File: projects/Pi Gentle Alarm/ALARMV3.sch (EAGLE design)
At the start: 9 parts, among them IC1 7805T, X1 RASPI_BOARD_B+_E0

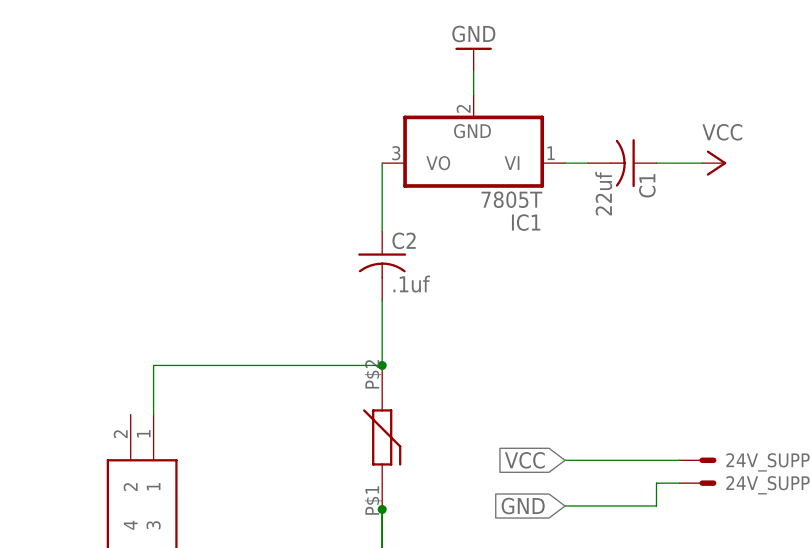
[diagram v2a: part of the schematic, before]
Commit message: Removed extra components
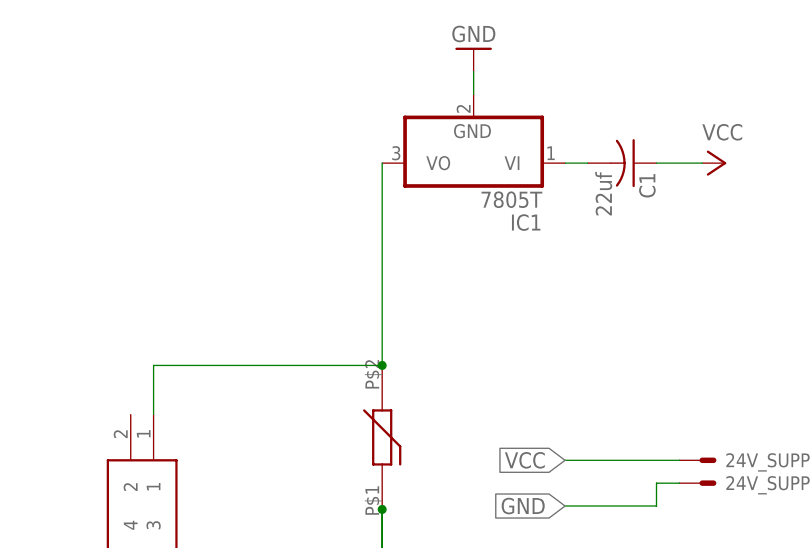
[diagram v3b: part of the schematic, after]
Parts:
- removed C2: .1uf, adafruit:C-US050-024X044
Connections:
- removed net N$2: C2.2, F1.P$2, S1.1
- net N$5: now also F1.P$2, S1.1; no longer C2.1
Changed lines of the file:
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@@
 <part name="S1" library="SamacSys_Parts" deviceset="2-1825910-7" device=""/>
 <part name="C1" library="adafruit" library_urn="urn:adsk.eagle:library:420" deviceset="C-US" device="050-024X044" package3d_urn="urn:adsk.eagle:package:6240356/1" value="22uf"/>
-<part name="C2" library="adafruit" library_urn="urn:adsk.eagle:library:420" deviceset="C-US" device="050-024X044" package3d_urn="urn:adsk.eagle:package:6240356/1" value=".1uf"/>
 </parts>
 <sheets>
@@
 <attribute name="VALUE" x="107.569" y="230.124" size="1.778" layer="96" rot="R270"/>
 </instance>
-<instance part="C2" gate="G$1" x="83.82" y="220.98" smashed="yes">
-<attribute name="NAME" x="84.836" y="221.615" size="1.778" layer="95"/>
-<attribute name="VALUE" x="84.836" y="216.789" size="1.778" layer="96"/>
-</instance>
 </instances>
 <busses>
@@
 </segment>
 </net>
-<net name="N$2" class="0">
-<segment>
-<wire x1="83.82" y1="208.28" x2="83.82" y2="208.66" width="0.1524" layer="91"/>
-<pinref part="F1" gate="G$1" pin="P$2"/>
-<junction x="83.82" y="208.66"/>
-<pinref part="S1" gate="G$1" pin="1"/>
-<wire x1="83.82" y1="208.66" x2="58.42" y2="208.66" width="0.1524" layer="91"/>
-<wire x1="58.42" y1="208.66" x2="58.42" y2="203.2" width="0.1524" layer="91"/>
-<pinref part="C2" gate="G$1" pin="2"/>
-<wire x1="83.82" y1="215.9" x2="83.82" y2="208.66" width="0.1524" layer="91"/>
-</segment>
-</net>
 <net name="N$3" class="0">
 <segment>
@@
 <segment>
 <pinref part="IC1" gate="A1" pin="VO"/>
-<pinref part="C2" gate="G$1" pin="1"/>
-<wire x1="83.82" y1="231.14" x2="83.82" y2="223.52" width="0.1524" layer="91"/>
+<wire x1="83.82" y1="208.28" x2="83.82" y2="208.66" width="0.1524" layer="91"/>
+<pinref part="F1" gate="G$1" pin="P$2"/>
+<junction x="83.82" y="208.66"/>
+<pinref part="S1" gate="G$1" pin="1"/>
+<wire x1="83.82" y1="208.66" x2="58.42" y2="208.66" width="0.1524" layer="91"/>
+<wire x1="58.42" y1="208.66" x2="58.42" y2="203.2" width="0.1524" layer="91"/>
+<wire x1="83.82" y1="231.14" x2="83.82" y2="208.66" width="0.1524" layer="91"/>
 </segment>
 </net>

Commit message: Added a part
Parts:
- removed Q1: (no value), transistors:2N7000_TO92
- added IC2: STP14NF10, SamacSys_Parts:STP14NF10
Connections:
- net GND: now also IC2.S; no longer Q1.S
- net GPIO17: now also IC2.G; no longer Q1.G
- net N$6: now also IC2.2; no longer Q1.D
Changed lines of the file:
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@@
 <?xml version="1.0" encoding="utf-8"?>
 <!DOCTYPE eagle SYSTEM "eagle.dtd">
-<eagle version="9.5.0">
+<eagle version="9.5.1">
 <drawing>
 <settings>
@@
 </part>
 <part name="24V_SUPPLY" library="con-molex" library_urn="urn:adsk.eagle:library:165" deviceset="22-23-2021" device="" package3d_urn="urn:adsk.eagle:package:8078633/1"/>
-<part name="Q1" library="transistors" deviceset="2N700*" device="_TO92" technology="0">
-<attribute name="MF" value=""/>
-<attribute name="MPN" value="2N7000."/>
-<attribute name="OC_NEWARK" value="26AC6371"/>
-</part>
 <part name="P+1" library="supply1" library_urn="urn:adsk.eagle:library:371" deviceset="VCC" device=""/>
 <part name="GND1" library="supply1" library_urn="urn:adsk.eagle:library:371" deviceset="GND" device=""/>
@@
 <part name="S1" library="SamacSys_Parts" deviceset="2-1825910-7" device=""/>
 <part name="C1" library="adafruit" library_urn="urn:adsk.eagle:library:420" deviceset="C-US" device="050-024X044" package3d_urn="urn:adsk.eagle:package:6240356/1" value="22uf"/>
+<part name="IC2" library="SamacSys_Parts" deviceset="STP14NF10" device=""/>
 </parts>
 <sheets>
@@
 <attribute name="NAME" x="121.92" y="194.818" size="1.524" layer="95"/>
 </instance>
-<instance part="Q1" gate="G$1" x="22.86" y="167.64" smashed="yes" rot="R180">
-<attribute name="NAME" x="16.256" y="166.878" size="1.778" layer="95" rot="R180"/>
-<attribute name="VALUE" x="16.256" y="169.164" size="1.778" layer="96" rot="R180"/>
-<attribute name="OC_NEWARK" x="22.86" y="167.64" size="1.778" layer="96" display="off"/>
-<attribute name="MF" x="22.86" y="167.64" size="1.778" layer="96" display="off"/>
-<attribute name="MPN" x="22.86" y="167.64" size="1.778" layer="96" display="off"/>
-</instance>
 <instance part="P+1" gate="VCC" x="22.86" y="127" smashed="yes" rot="R180">
 <attribute name="VALUE" x="25.4" y="129.54" size="1.778" layer="96" rot="R270"/>
@@
 <attribute name="VALUE" x="107.569" y="230.124" size="1.778" layer="96" rot="R270"/>
 </instance>
+<instance part="IC2" gate="G$1" x="25.4" y="157.48" smashed="yes" rot="MR90">
+<attribute name="NAME" x="33.02" y="173.99" size="1.778" layer="95" rot="MR90" align="center-left"/>
+<attribute name="VALUE" x="30.48" y="173.99" size="1.778" layer="96" rot="MR90" align="center-left"/>
+</instance>
 </instances>
 <busses>
@@
 </segment>
 <segment>
-<pinref part="Q1" gate="G$1" pin="S"/>
 <pinref part="GND1" gate="1" pin="GND"/>
 <wire x1="22.86" y1="177.8" x2="22.86" y2="180.34" width="0.1524" layer="91"/>
+<pinref part="IC2" gate="G$1" pin="S"/>
+<wire x1="22.86" y1="177.8" x2="25.4" y2="177.8" width="0.1524" layer="91"/>
 </segment>
 <segment>
@@
 <segment>
 <wire x1="73.66" y1="170.18" x2="33.02" y2="170.18" width="0.1524" layer="91"/>
-<pinref part="Q1" gate="G$1" pin="G"/>
 <pinref part="X1" gate="G$1" pin="GPIO17"/>
+<pinref part="IC2" gate="G$1" pin="G"/>
+<wire x1="33.02" y1="170.18" x2="33.02" y2="157.48" width="0.1524" layer="91"/>
+<wire x1="33.02" y1="157.48" x2="25.4" y2="157.48" width="0.1524" layer="91"/>
 </segment>
 </net>
 <net name="N$6" class="0">
 <segment>
-<pinref part="Q1" gate="G$1" pin="D"/>
 <wire x1="22.86" y1="152.4" x2="22.86" y2="157.48" width="0.1524" layer="91"/>
 <pinref part="LED1" gate="G$1" pin="A"/>
+<pinref part="IC2" gate="G$1" pin="2"/>
 </segment>
 </net>
